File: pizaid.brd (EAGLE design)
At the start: 44 parts, among them X1 S4B-ZR, X2 DCJACK-R

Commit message: ぐらんどきれいにした
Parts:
- R11: value (none) -> 10k
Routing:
- net GND: track 385.3 -> 380.9 mm
- net 5V0@2: track 145.3 -> 144.5 mm
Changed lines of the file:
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@@
 <attribute name="OC_FARNELL" value="9491830" x="40.225" y="52.3425" size="1.778" layer="28" rot="MR180" display="off"/>
 </element>
-<element name="R11" library="rcl" package="R0603" value="" x="50.3975" y="41.69" rot="R270"/>
+<element name="R11" library="rcl" package="R0603" value="10k" x="50.3975" y="41.69" rot="R270"/>
 <element name="U$8" library="pizaid" package="B2P-VH" value="B2P-VH" x="16.5625" y="29.375" rot="R270"/>
 <element name="U$9" library="pizaid" package="B2P-VH" value="B2P-VH" x="16.5625" y="10" rot="R270"/>
@@
 <wire x1="41.4475" y1="30.4275" x2="41.875" y2="30" width="2" layer="1"/>
 <wire x1="41.875" y1="30" x2="48.4375" y2="30" width="2" layer="1"/>
-<via x="48.4375" y="30" extent="1-16" drill="1"/>
-<wire x1="48.4375" y1="30" x2="48.4375" y2="5.625" width="2" layer="16"/>
-<via x="48.4375" y="5.625" extent="1-16" drill="1"/>
+<via x="48.4375" y="30" extent="1-16" drill="1" diameter="1.5"/>
 <wire x1="31.6325" y1="26.71" x2="36.3975" y2="26.71" width="0.6" layer="1"/>
 <wire x1="36.3975" y1="26.71" x2="37.1875" y2="27.5" width="0.6" layer="1"/>
@@
 <wire x1="69.6" y1="28.5" x2="69.6" y2="30.9375" width="0.6" layer="1"/>
 <wire x1="69.6" y1="30.9375" x2="73.075" y2="30.9375" width="0.6" layer="1"/>
-<wire x1="48.4375" y1="5.625" x2="34.6875" y2="5.625" width="2" layer="1"/>
+<wire x1="56.25" y1="5.625" x2="34.6875" y2="5.625" width="2" layer="1"/>
 <wire x1="34.6875" y1="5.625" x2="30.625" y2="9.6875" width="2" layer="1"/>
 <wire x1="30.625" y1="9.6875" x2="30.625" y2="13.125" width="2" layer="1"/>
@@
 <wire x1="73.58" y1="49.6625" x2="73.58" y2="53.295" width="2" layer="1"/>
 <wire x1="25.625" y1="34.0625" x2="30" y2="34.0625" width="2" layer="1"/>
-<wire x1="48.4375" y1="5.625" x2="56.25" y2="5.625" width="2" layer="1"/>
 <wire x1="56.25" y1="5.625" x2="58.645" y2="8.02" width="2" layer="1"/>
 <wire x1="58.645" y1="10.25" x2="58.645" y2="8.02" width="2" layer="1"/>
 <wire x1="58.645" y1="10.25" x2="58.645" y2="13.02" width="2" layer="1"/>
-<wire x1="58.645" y1="13.02" x2="73.075" y2="27.45" width="2" layer="1"/>
+<wire x1="58.645" y1="13.02" x2="63.4375" y2="17.8125" width="2" layer="1"/>
+<wire x1="63.59375" y1="17.96875" x2="73.075" y2="27.45" width="2" layer="1"/>
 <wire x1="69.6" y1="28.5" x2="71" y2="28.5" width="0.6" layer="1"/>
 <wire x1="71" y1="28.5" x2="71.25" y2="28.75" width="0.6" layer="1"/>
@@
 <wire x1="11.1875" y1="51.5625" x2="11.1875" y2="49.7625" width="2" layer="1"/>
 <wire x1="11.1875" y1="49.7625" x2="14.1875" y2="46.7625" width="2" layer="1"/>
-<wire x1="41.875" y1="30" x2="40.625" y2="27.5" width="0" layer="19" extent="1-1"/>
+<wire x1="48.4375" y1="30" x2="60.625" y2="17.8125" width="2" layer="16"/>
+<wire x1="60.625" y1="17.8125" x2="61.875" y2="17.8125" width="2" layer="16"/>
+<via x="61.875" y="17.8125" extent="1-16" drill="1" diameter="1.4"/>
+<wire x1="61.875" y1="17.8125" x2="63.4375" y2="17.8125" width="2" layer="1"/>
+<wire x1="63.4375" y1="17.8125" x2="63.59375" y2="17.96875" width="2" layer="1"/>
 </signal>
 <signal name="VCC">
@@
 <wire x1="16.5625" y1="21.6675" x2="27.0825" y2="21.6675" width="2" layer="1"/>
 <wire x1="27.0825" y1="21.6675" x2="33.125" y2="15.625" width="2" layer="1"/>
-<wire x1="35.67" y1="10.2625" x2="35.67" y2="8.3925" width="0.6" layer="1"/>
-<wire x1="35.67" y1="8.3925" x2="36.25" y2="7.8125" width="0.6" layer="1"/>
-<wire x1="36.25" y1="7.8125" x2="50" y2="7.8125" width="0.6" layer="1"/>
-<wire x1="50" y1="7.8125" x2="51.875" y2="9.6875" width="0.6" layer="1"/>
-<wire x1="51.875" y1="9.6875" x2="51.875" y2="12.5" width="0.6" layer="1"/>
-<wire x1="51.875" y1="12.5" x2="52.5" y2="13.125" width="0.6" layer="1"/>
-<via x="52.5" y="13.125" extent="1-16" drill="0.8" diameter="1.4"/>
-<wire x1="52.5" y1="13.125" x2="60" y2="13.125" width="0.6" layer="16"/>
 <wire x1="60" y1="13.125" x2="62.1875" y2="10.9375" width="0.6" layer="16"/>
+<wire x1="60" y1="13.125" x2="36.5625" y2="13.125" width="0.6" layer="16"/>
+<wire x1="36.5625" y1="13.125" x2="33.75" y2="10.3125" width="0.6" layer="16"/>
+<via x="33.75" y="10.3125" extent="1-16" drill="0.8" diameter="1.4"/>
+<wire x1="33.75" y1="10.3125" x2="35.62" y2="10.3125" width="0.6" layer="1"/>
+<wire x1="35.62" y1="10.3125" x2="35.7325" y2="10.2" width="0.6" layer="1"/>
 </signal>
 <signal name="N$9">

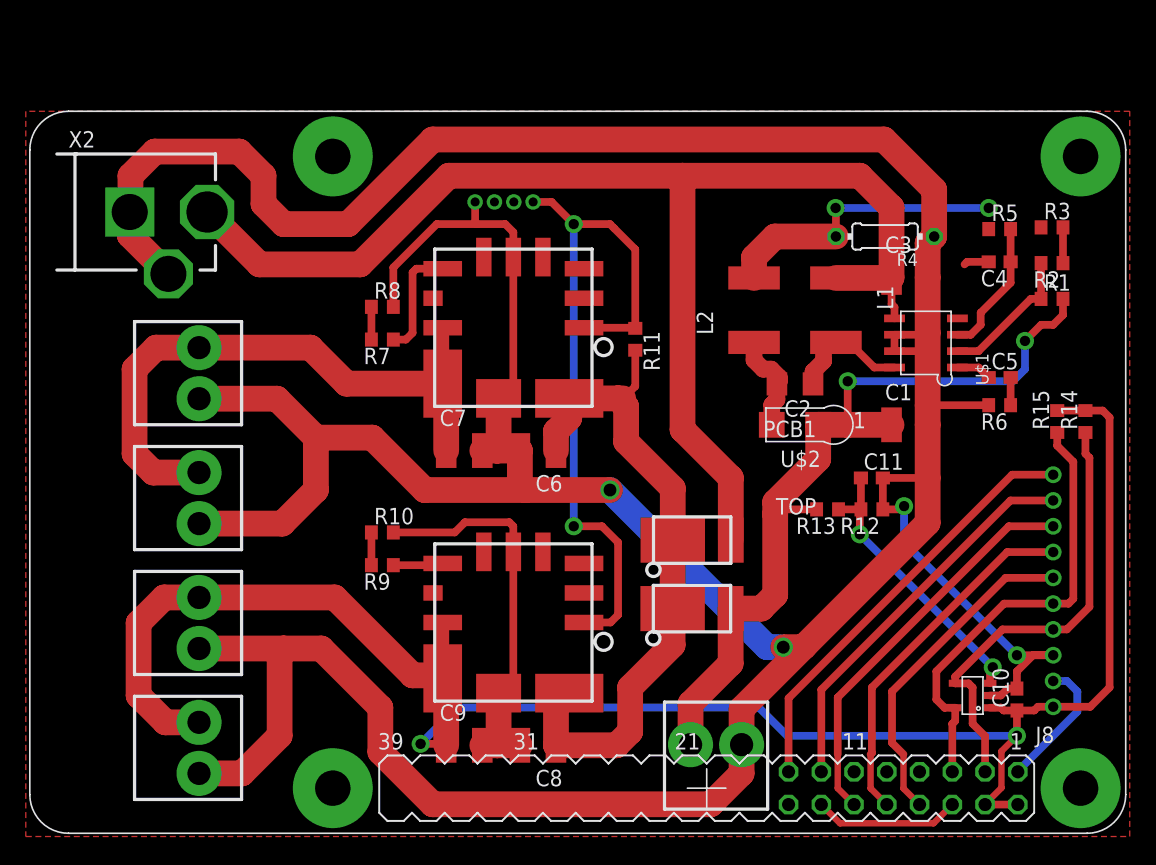
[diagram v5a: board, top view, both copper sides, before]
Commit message: modified board outline
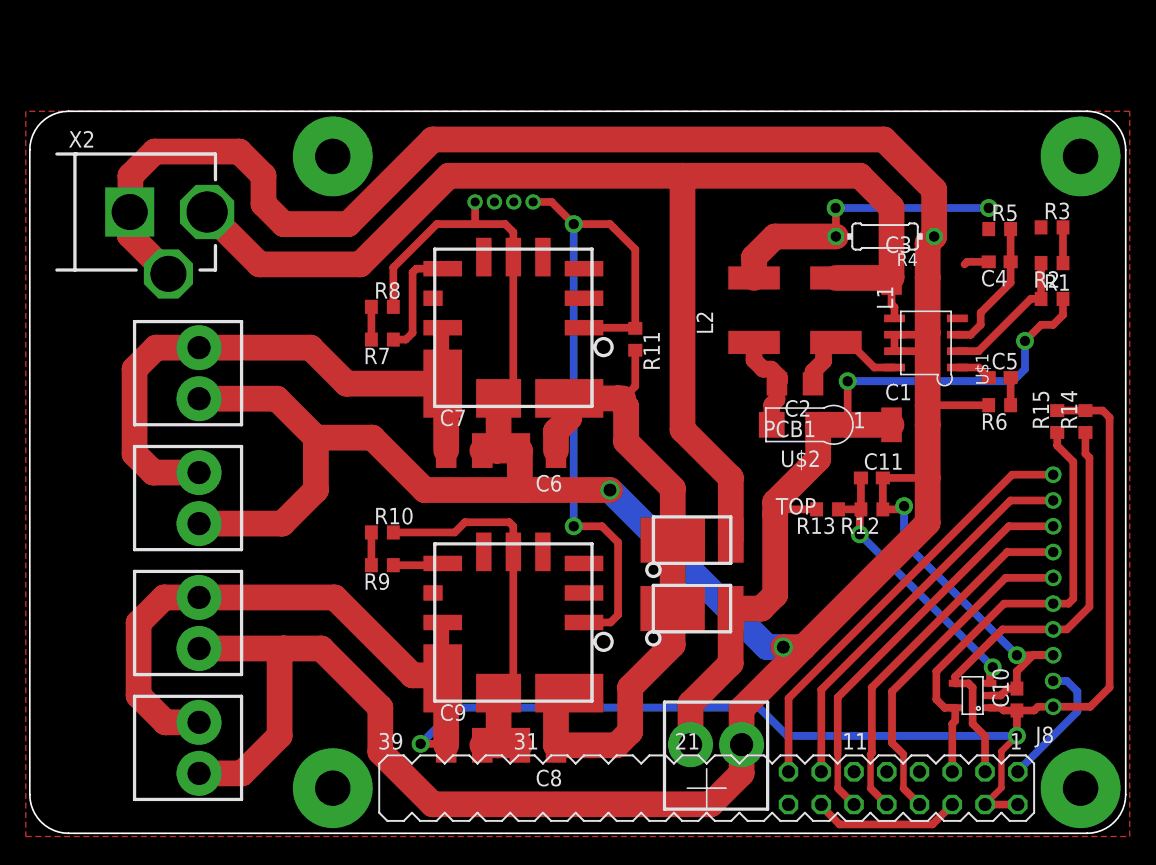
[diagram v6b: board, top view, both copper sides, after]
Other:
- board outline added: 85 x 56 mm
